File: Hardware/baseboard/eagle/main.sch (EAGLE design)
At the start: 29 parts, among them P2 NTC, P3 BATTERY, X1.2 TACH/LAP, X2.1 MOTOR, X2.2 VRAILS+, X2.3 5V+SoC

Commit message: quicksave: finalized some component values/footprints (thx @kerash) + fixed battery connector (also gone with the 4pos, can populate 3pos/2pos + wires) + verified some schematic elements with @kerash + added some missing control signals to bias later today
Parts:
- removed P2: NTC, kitt.con:S2B-PH-K-S(LF)(SN)
- removed P3: BATTERY, kitt.con:S2B-PH-K-S(LF)(SN)
- added X1: JST-4POS-2X4POS, kitt.con:JST-4POS-2X4POS
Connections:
- net ENC renamed CTRL.ENC
- net N$12 renamed !RST
- removed net DDC.VOUT: L2.2
- removed net FB: ☇1.TP
- removed net N$32: P3.2, S1.1
- removed net N$6: P2.2
- removed net VOUT: L2.1, ☇2.TP
- new net TOP.BAT+NTC: X1B.1
- new net TOP.BAT/CON: S1.1, X1A.1
- net GND: now also X1A.2, X1B.2; no longer P2.1, P3.1
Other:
- note added: "CONFIGURATION BIAS"
- note added: "DUMB"
- note added: "ROUTING"
- note added: "[CAP MISSING?]"
- note added: "[TODO REDO TOP]"
- note added: "[TODO10]"
- note added: "[TODO10] https://github.com/NextThingCo/CHIP-Hardware/blob/master/CHIP[v1_0]/CHIP_v1_0_SCHEMATIC_20151203.pdf Look at Battery In: Capacitor and ESD38, what's this?"
- note added: "[domh]"
- note added: "[kerash]"
- note added: "[spec1]"
- note added: "[spec1]: Low ESR, OP~5V,ceramic"
- note added: "{H}"
- note removed: "LAYOUT MASTER"
- note removed: "LOW ESR"
- note removed: "NOTE: Make Breakout for MCP dual purpose: -> credit card sized, with indicator LED and switch breakaway -> also has hexswitch for adress select -> can use as an actual tool or as submod"
- note removed: "TODO: Replace all packages of passives (currently non-smt)"
- note removed: "TODO: use 4pol using standard 4-wire scheme -> can populate with 2pol and hardwire ntc instead"
- note removed: "USE ONLY WITH >IMPORT EAGLE DRAWING< COMMAND"
- note removed: "[ ] Check proximity constraints for passives -> Application Note [ ] Important: Double check values and omittables!!! also LB and FB! [ ] Pullups: To which potential? 3V3 seems really fishy, given it comes from the SoC. [ ] Name nets on pins after pins connected for routing later, maybe use some unicode symbol for proximity constraints?"
- note removed: "[TODO4]: This should work, but in practice this will wreck the routing -> investigate about the control inputs on all DC/DC converters"
- note removed: "peak 4-6A"

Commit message: quicksave: progress was made \w the LTC4000 subunit  + taking my 15
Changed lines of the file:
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@@
 </busses>
 <nets>
-<net name="DDC.VIN" class="0">
+<net name="DDC.CLN/VIN" class="0">
 <segment>
 <portref moduleinst="A6" port="DDC.VIN"/>

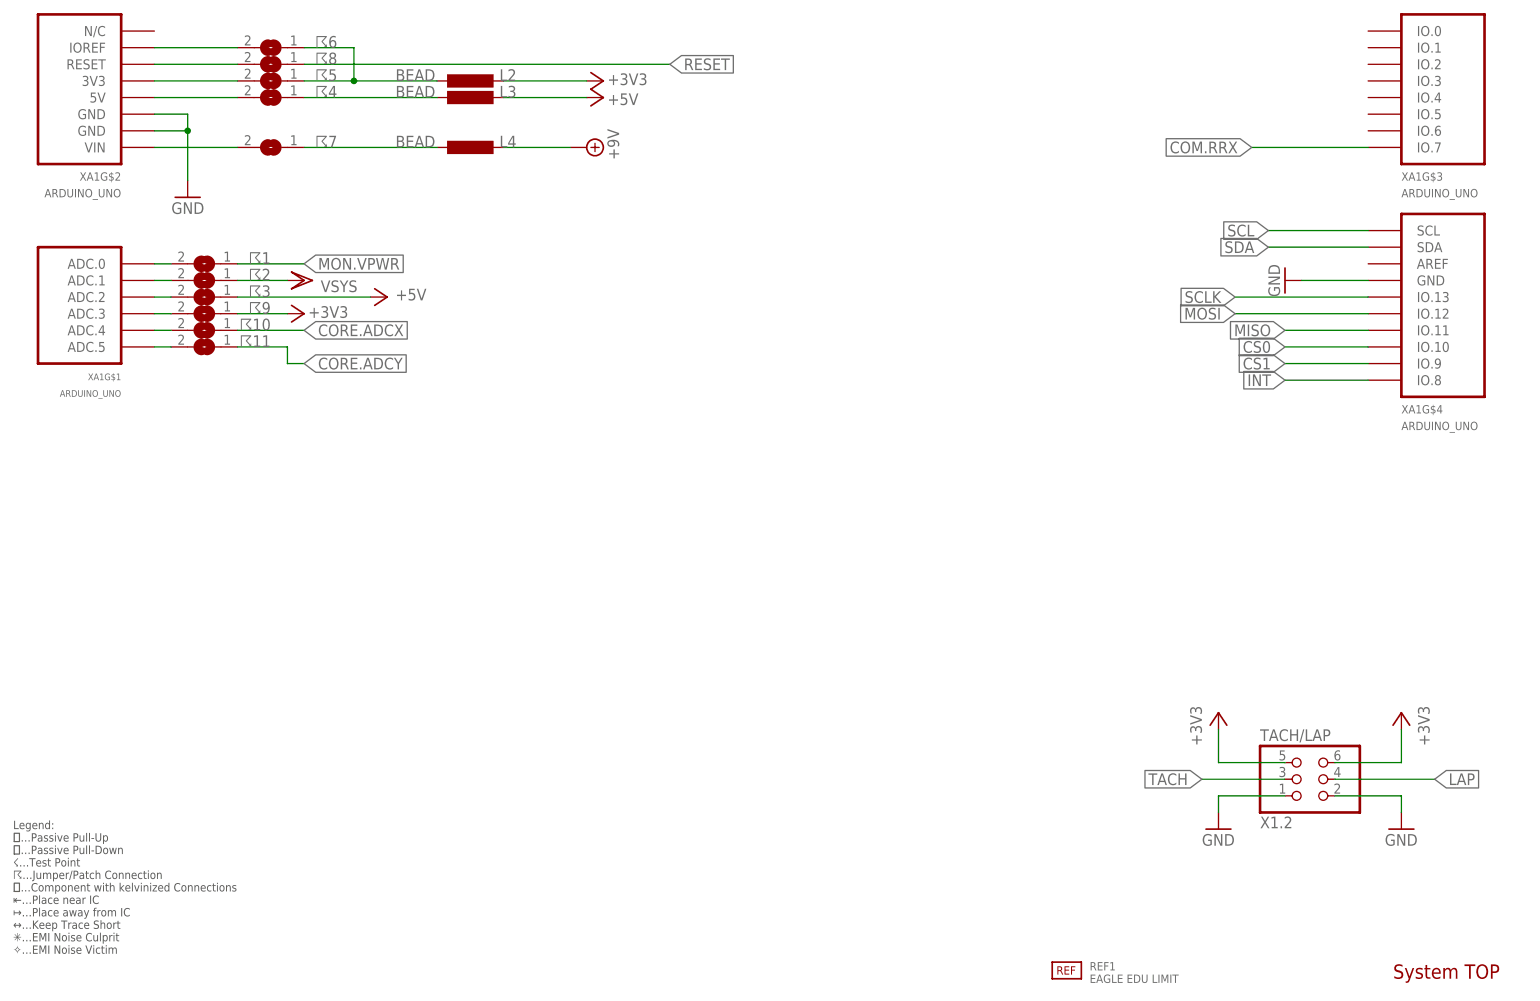
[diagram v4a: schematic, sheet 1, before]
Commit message: board layout WIP +moved around some connectors +will now do the 5V dcdc to make sure everything fits
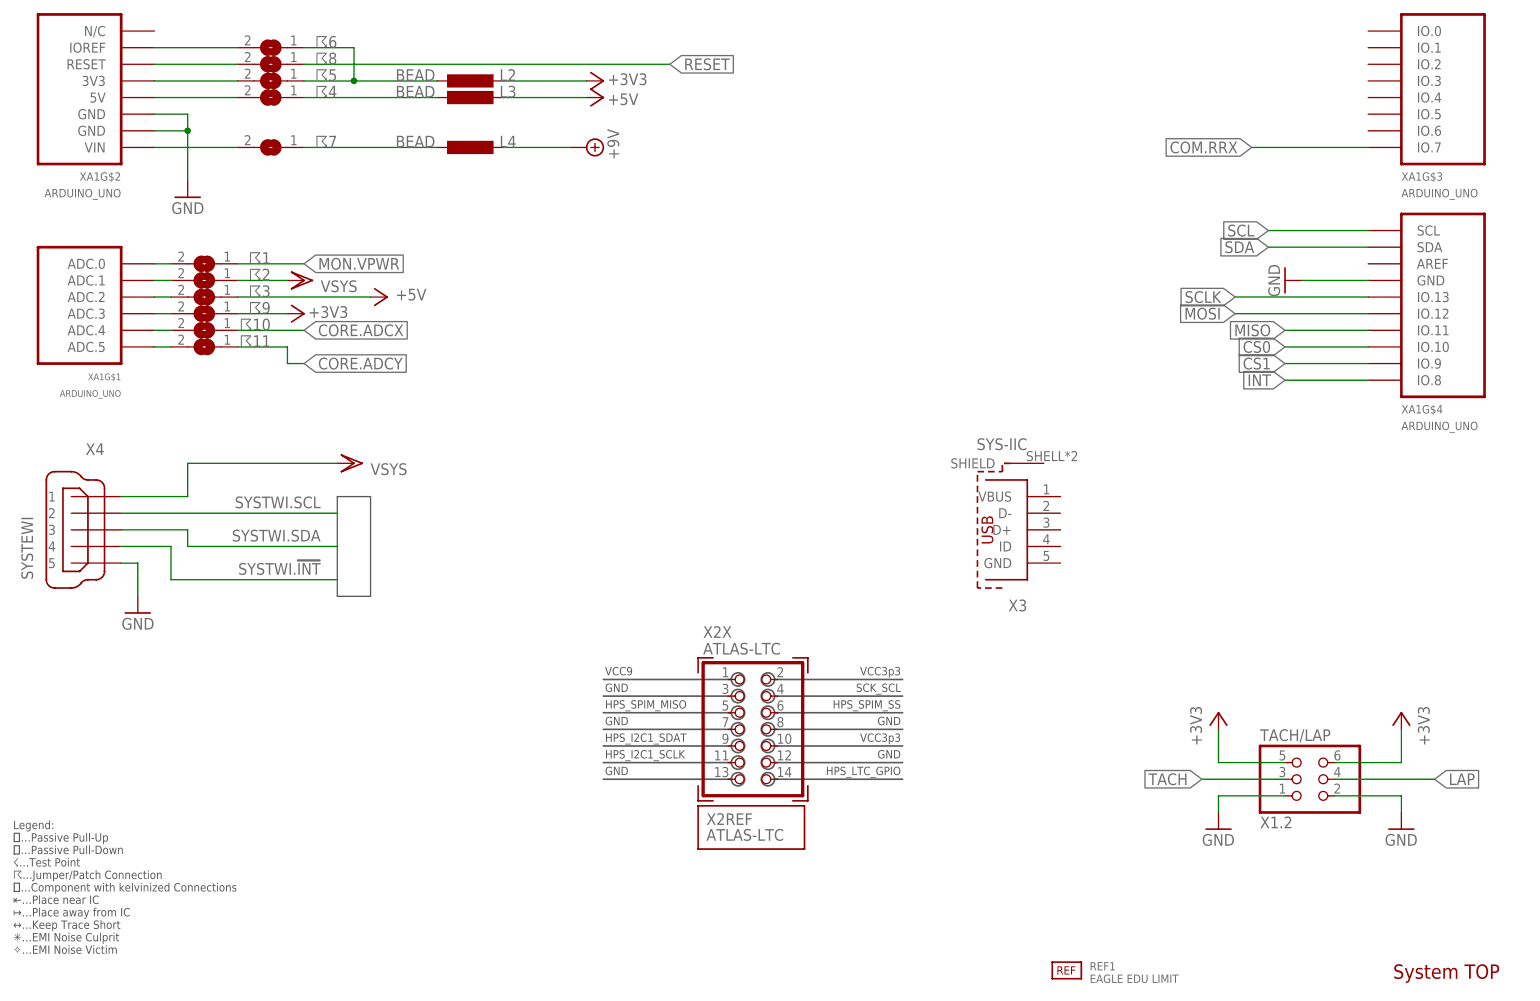
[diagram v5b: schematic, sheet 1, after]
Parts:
- added X2: ATLAS-LTC, kitt.con:ROCKETBOARDS-LTCTH
- added X3: SYS-IIC, kitt.con:WüRTH-MINIB.VERTICAL
- added X4: SYSTEWI, con-cypressindustries:MINI-USB_SHIELD5P2-32005-601
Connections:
- new net SYSTWI.!INT: X4G41.4
- new net SYSTWI.SCL: X4G41.2
- new net SYSTWI.SDA: X4G41.3
- net GND: now also X4G41.5
- net VDD: now also X4G41.1
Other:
- note added: "[an02]"
- note added: "[an02]: Optional Current Programming Resistor Populate with Capacitor and fitting value"
- note added: "i thought it's an for annotation"
- note added: "wait what? who did this? Is that you anton?"

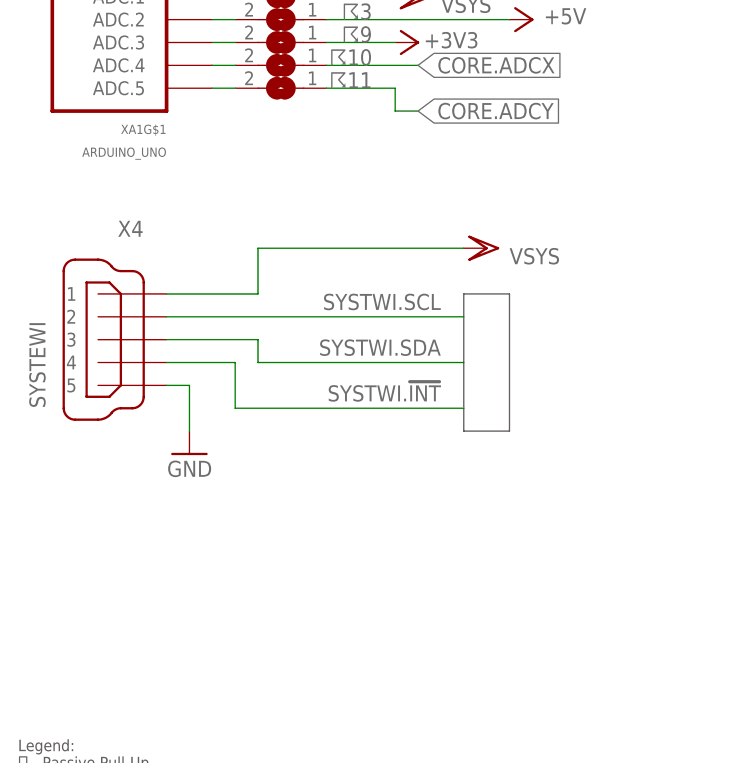
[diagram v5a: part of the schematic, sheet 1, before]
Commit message: baseboard wip +did layout for 5V DCDC, was really fun to do, TI know their sh…tuff +now integrating into baseboard
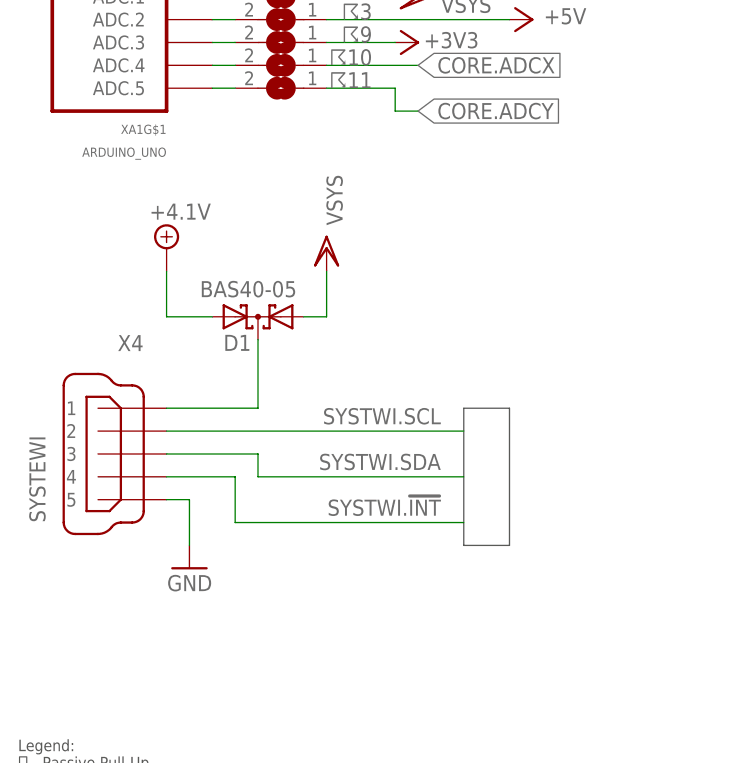
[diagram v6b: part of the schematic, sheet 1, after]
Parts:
- added D1: BAS40-05, diode:BAS40-05
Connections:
- removed net TOP.V+/IPC: S1.2
- new net +4.1V: D1.A2, S1.2
- new net N$1: D1.C, X4G41.1
- new net V~IN: D1.A
- new net ↔BOOST: D1.C
- new net ↔ILIM: D1.A
- net VDD: now also D1.A1; no longer X4G41.1
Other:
- note added: "[an01]"
- note added: "[an01]: polarity protection and voltage join; business as usual"
- moved on the sheet: S1, X4
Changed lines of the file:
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@@
 </segment>
 </net>
-<net name="N$1" class="0">
+<net name="CC" class="0">
 <segment>
 <pinref part="U1" gate="G$1" pin="CC"/>
@@
 <part name="GND5" library="supply1" deviceset="GND" device=""/>
 <part name="VDD6" library="supply1" deviceset="VDD" device="" value="VSYS"/>
+<part name="SUPPLY2" library="supply2" deviceset="+4.1V" device=""/>
+<part name="SUPPLY3" library="supply2" deviceset="+4.1V" device=""/>
+<part name="D1" library="diode" deviceset="BAS40-05" device=""/>
 </parts>
 <sheets>
@@
 <text x="0" y="-45.72" size="5.08" layer="98">✔</text>
 <text x="0" y="-50.8" size="5.08" layer="98">✔</text>
-<text x="58.42" y="81.28" size="1.778" layer="98" ratio="20" rot="R90" align="center-left">SYSTWI</text>
+<text x="58.42" y="68.58" size="1.778" layer="98" ratio="20" rot="R90" align="center-left">SYSTWI</text>
+<text x="35.56" y="86.36" size="1.778" layer="98" ratio="20" align="center-left">[an01]</text>
+<text x="160.02" y="35.56" size="1.778" layer="98" ratio="20" align="center-left">[an01]: polarity protection
+and voltage join; business as usual</text>
 </plain>
 <instances>
@@
 <instance part="X2" gate="REF" x="118.11" y="58.42"/>
 <instance part="X3" gate="G$1" x="158.75" y="88.9" rot="R180"/>
-<instance part="X4" gate="G41" x="17.78" y="88.9" rot="MR0"/>
-<instance part="GND5" gate="1" x="25.4" y="76.2" rot="MR0"/>
-<instance part="VDD6" gate="G$1" x="58.42" y="99.06" smashed="yes" rot="MR90">
-<attribute name="VALUE" x="60.96" y="99.06" size="1.778" layer="96" rot="MR180"/>
-</instance>
+<instance part="X4" gate="G41" x="17.78" y="76.2" rot="MR0"/>
+<instance part="GND5" gate="1" x="25.4" y="63.5" rot="MR0"/>
+<instance part="VDD6" gate="G$1" x="40.64" y="99.06" smashed="yes" rot="MR0">
+<attribute name="VALUE" x="40.64" y="101.6" size="1.778" layer="96" rot="MR90"/>
+</instance>
+<instance part="SUPPLY3" gate="P" x="22.86" y="99.06"/>
+<instance part="D1" gate="G$1" x="33.02" y="91.44" rot="R180"/>
 </instances>
 <busses>
 <bus name="TOP[0..7],SYSTWI.SCL,SYSTWI.SDA,SYSTWI.!INT,TOP.!RST">
 <segment>
-<wire x1="60.96" y1="78.74" x2="55.88" y2="78.74" width="0.762" layer="92"/>
-<wire x1="55.88" y1="78.74" x2="55.88" y2="93.98" width="0.762" layer="92"/>
-<wire x1="55.88" y1="93.98" x2="60.96" y2="93.98" width="0.762" layer="92"/>
-<wire x1="60.96" y1="93.98" x2="60.96" y2="78.74" width="0.762" layer="92"/>
+<wire x1="60.96" y1="66.04" x2="55.88" y2="66.04" width="0.762" layer="92"/>
+<wire x1="55.88" y1="66.04" x2="55.88" y2="81.28" width="0.762" layer="92"/>
+<wire x1="55.88" y1="81.28" x2="60.96" y2="81.28" width="0.762" layer="92"/>
+<wire x1="60.96" y1="81.28" x2="60.96" y2="66.04" width="0.762" layer="92"/>
 </segment>
 </bus>
@@
 <pinref part="X4" gate="G41" pin="5"/>
 <pinref part="GND5" gate="1" pin="GND"/>
-<wire x1="22.86" y1="83.82" x2="25.4" y2="83.82" width="0.1524" layer="91"/>
-<wire x1="25.4" y1="83.82" x2="25.4" y2="78.74" width="0.1524" layer="91"/>
+<wire x1="22.86" y1="71.12" x2="25.4" y2="71.12" width="0.1524" layer="91"/>
+<wire x1="25.4" y1="71.12" x2="25.4" y2="66.04" width="0.1524" layer="91"/>
 </segment>
 </net>
@@
 <segment>
 <pinref part="X4" gate="G41" pin="4"/>
-<wire x1="22.86" y1="86.36" x2="30.48" y2="86.36" width="0.1524" layer="91"/>
-<wire x1="30.48" y1="86.36" x2="30.48" y2="81.28" width="0.1524" layer="91"/>
-<wire x1="30.48" y1="81.28" x2="55.88" y2="81.28" width="0.1524" layer="91"/>
-<label x="53.34" y="83.82" size="1.778" layer="95" ratio="20" rot="R180"/>
+<wire x1="22.86" y1="73.66" x2="30.48" y2="73.66" width="0.1524" layer="91"/>
+<wire x1="30.48" y1="73.66" x2="30.48" y2="68.58" width="0.1524" layer="91"/>
+<wire x1="30.48" y1="68.58" x2="55.88" y2="68.58" width="0.1524" layer="91"/>
+<label x="53.34" y="71.12" size="1.778" layer="95" ratio="20" rot="R180"/>
 </segment>
 </net>
@@
 <segment>
 <pinref part="X4" gate="G41" pin="3"/>
-<wire x1="22.86" y1="88.9" x2="33.02" y2="88.9" width="0.1524" layer="91"/>
-<wire x1="33.02" y1="88.9" x2="33.02" y2="86.36" width="0.1524" layer="91"/>
-<wire x1="33.02" y1="86.36" x2="55.88" y2="86.36" width="0.1524" layer="91"/>
-<label x="53.34" y="88.9" size="1.778" layer="95" ratio="20" rot="R180"/>
+<wire x1="22.86" y1="76.2" x2="33.02" y2="76.2" width="0.1524" layer="91"/>
+<wire x1="33.02" y1="76.2" x2="33.02" y2="73.66" width="0.1524" layer="91"/>
+<wire x1="33.02" y1="73.66" x2="55.88" y2="73.66" width="0.1524" layer="91"/>
+<label x="53.34" y="76.2" size="1.778" layer="95" ratio="20" rot="R180"/>
 </segment>
 </net>
@@
 <segment>
 <pinref part="X4" gate="G41" pin="2"/>
-<wire x1="22.86" y1="91.44" x2="55.88" y2="91.44" width="0.1524" layer="91"/>
-<label x="53.34" y="93.98" size="1.778" layer="95" ratio="20" rot="R180"/>
+<wire x1="22.86" y1="78.74" x2="55.88" y2="78.74" width="0.1524" layer="91"/>
+<label x="53.34" y="81.28" size="1.778" layer="95" ratio="20" rot="R180"/>
+</segment>
+</net>
+<net name="N$1" class="0">
+<segment>
+<pinref part="X4" gate="G41" pin="1"/>
+<wire x1="22.86" y1="81.28" x2="33.02" y2="81.28" width="0.1524" layer="91"/>
+<wire x1="33.02" y1="81.28" x2="33.02" y2="88.9" width="0.1524" layer="91"/>
+<pinref part="D1" gate="G$1" pin="C"/>
+</segment>
+</net>
+<net name="+4.1V" class="0">
+<segment>
+<pinref part="SUPPLY3" gate="P" pin="+4.1V"/>
+<pinref part="D1" gate="G$1" pin="A2"/>
+<wire x1="22.86" y1="96.52" x2="22.86" y2="91.44" width="0.1524" layer="91"/>
+<wire x1="22.86" y1="91.44" x2="27.94" y2="91.44" width="0.1524" layer="91"/>
 </segment>
 </net>
 <net name="VDD" class="0">
 <segment>
-<pinref part="X4" gate="G41" pin="1"/>
-<wire x1="22.86" y1="93.98" x2="33.02" y2="93.98" width="0.1524" layer="91"/>
 <pinref part="VDD6" gate="G$1" pin="VDD"/>
-<wire x1="33.02" y1="93.98" x2="33.02" y2="99.06" width="0.1524" layer="91"/>
-<wire x1="33.02" y1="99.06" x2="55.88" y2="99.06" width="0.1524" layer="91"/>
+<pinref part="D1" gate="G$1" pin="A1"/>
+<wire x1="40.64" y1="96.52" x2="40.64" y2="91.44" width="0.1524" layer="91"/>
+<wire x1="40.64" y1="91.44" x2="38.1" y2="91.44" width="0.1524" layer="91"/>
 </segment>
 </net>
@@
 <text x="313.69" y="49.53" size="1.778" layer="115" ratio="20" align="center-left">[domh]</text>
 <text x="313.69" y="69.85" size="1.778" layer="115" ratio="20" align="center-left">[domh]</text>
-<text x="266.7" y="66.04" size="1.778" layer="115" ratio="20" align="center-left">[domh]</text>
+<text x="274.32" y="66.04" size="1.778" layer="115" ratio="20" align="center-left">[domh]</text>
 <text x="312.42" y="78.74" size="1.778" layer="98" ratio="20" align="center-left">[TODO10]</text>
 <text x="256.54" y="-7.62" size="1.778" layer="98" ratio="20" align="center-left">[TODO10]
@@
 </instance>
 <instance part="S3" gate="G$1" x="160.02" y="129.54" rot="MR0"/>
-<instance part="S1" gate="G$1" x="270.51" y="66.04"/>
+<instance part="S1" gate="G$1" x="278.13" y="66.04"/>
 <instance part="P+4" gate="1" x="124.46" y="241.3" smashed="yes" rot="MR0">
 <attribute name="VALUE" x="123.19" y="242.57" size="1.778" layer="96" rot="MR90"/>
@@
 <instance part="X1" gate="A" x="314.96" y="69.85" rot="MR180"/>
 <instance part="X1" gate="B" x="314.96" y="49.53" rot="MR180"/>
+<instance part="SUPPLY2" gate="P" x="264.16" y="83.82"/>
 </instances>
 <busses>
@@
 </segment>
 </net>
-<net name="TOP.V+/IPC" class="0">
-<segment>
-<portref moduleinst="A5" port="BAT.+"/>
-<wire x1="256.54" y1="106.68" x2="256.54" y2="66.04" width="0.1524" layer="91"/>
-<pinref part="S1" gate="G$1" pin="2"/>
-<wire x1="260.35" y1="66.04" x2="256.54" y2="66.04" width="0.1524" layer="91"/>
-</segment>
-</net>
 <net name="PWR.MOTA" class="0">
 <segment>
@@
 <segment>
 <pinref part="S1" gate="G$1" pin="1"/>
-<wire x1="280.67" y1="68.58" x2="309.88" y2="68.58" width="0.1524" layer="91"/>
+<wire x1="288.29" y1="68.58" x2="309.88" y2="68.58" width="0.1524" layer="91"/>
 <label x="308.61" y="67.31" size="1.778" layer="95" ratio="20" rot="R180"/>
 <pinref part="X1" gate="A" pin="1"/>
@@
 </segment>
 </net>
+<net name="+4.1V" class="0">
+<segment>
+<portref moduleinst="A5" port="BAT.+"/>
+<wire x1="256.54" y1="106.68" x2="256.54" y2="66.04" width="0.1524" layer="91"/>
+<pinref part="S1" gate="G$1" pin="2"/>
+<wire x1="267.97" y1="66.04" x2="264.16" y2="66.04" width="0.1524" layer="91"/>
+<pinref part="SUPPLY2" gate="P" pin="+4.1V"/>
+<wire x1="264.16" y1="66.04" x2="256.54" y2="66.04" width="0.1524" layer="91"/>
+<wire x1="264.16" y1="81.28" x2="264.16" y2="66.04" width="0.1524" layer="91"/>
+<junction x="264.16" y="66.04"/>
+</segment>
+</net>
